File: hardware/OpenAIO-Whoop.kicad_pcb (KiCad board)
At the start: 6 copper layers, 30.3 x 30.3 mm, 250 parts, among them J1 U.FL, J10 M3, J13 M4, J2 +, J20 LED, J21 5V, J22 BZ-, J23 CAM, J24 5V, J25 GND, J26 VHD, J27 GND, J28 TX0, J29 RX0, J3 -, J31 USB, J32 CAM, J33 GND, J4 M1, J7 M2, Q26 AP1606, Q27 BC857BM, Q28 AP1606, Q29 AGM210MAP, Q30 AGM210MAP, Q31 AGM210MAP, Q32 AGM210MAP, Q33 AGM210MAP, Q34 AGM210MAP, Q35 AGM210MAP, Q36 AGM210MAP, Q37 AGM210MAP, Q38 AGM210MAP, Q39 AGM210MAP, Q40 AGM210MAP, SW1 SKUBAAE010, U1 INA186A3, U10 RP2354A, U11 BMI270, U12 TPS7A2018, U13 PY25Q128HA-DFH-IR, U14 SN74LVC1G3157, U15 TLV7031, U16 ESP32-PICO-V3, U18 SX1281, U19 RTC6705, U2 TPS61022, U20 SE5004L, U21 LP5912-3.3, U22 LP5907-2.85, U4 LP5912-3.3, U6 EFM8BB51F16I, U7 EFM8BB51F16I, U8 EFM8BB51F16I, U9 EFM8BB51F16I, X1 12MHz, X3 52MHz TCXO, X4 8MHz 10pF

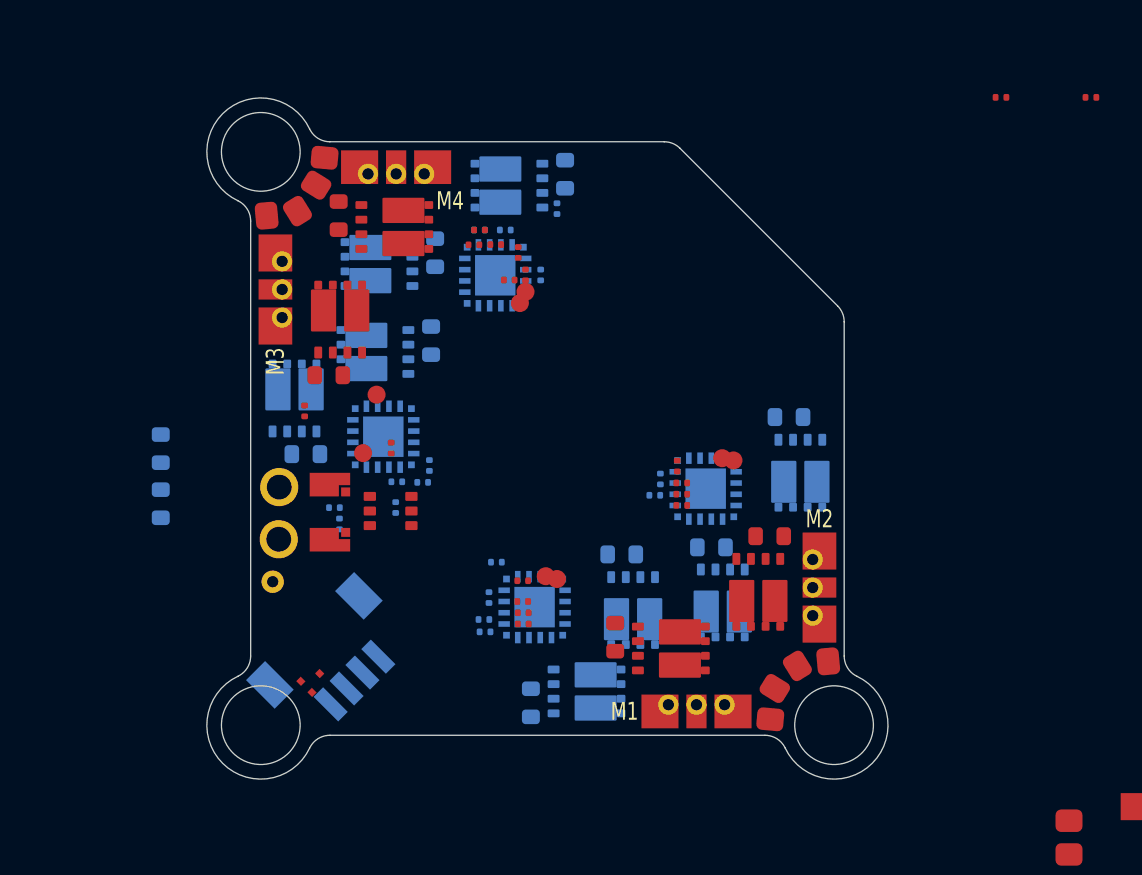
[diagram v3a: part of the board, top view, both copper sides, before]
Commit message: Owner routing checkpoint: ESC3 and ESC4 routed
Co-Authored-By: Claude Opus 5.5 <noreply@anthropic.com>
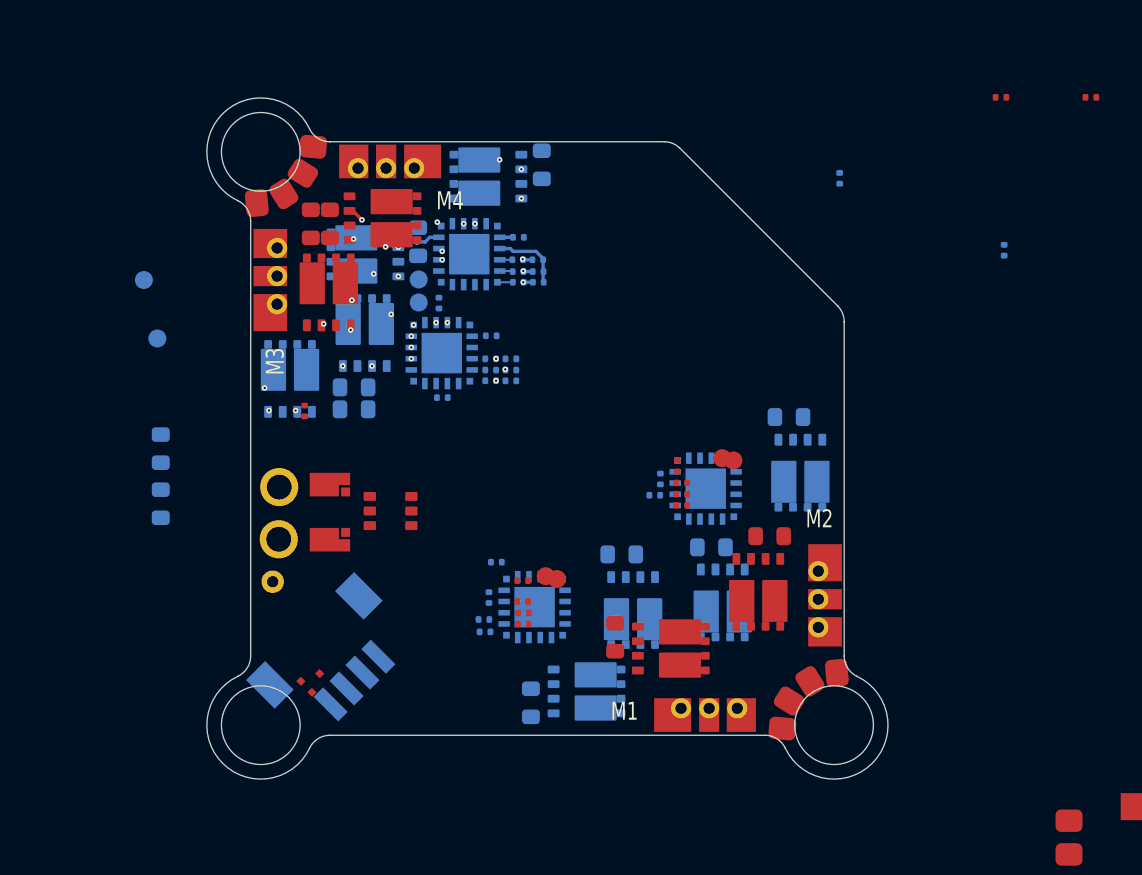
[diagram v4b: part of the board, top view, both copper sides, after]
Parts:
- C19, C31, Q37, R32, R34, R35, R38, R39, TP5, TP6, TP7, TP8: moved to B.Cu
- Q36: moved to F.Cu
- moved C25 20.6 mm to (133.5, 104.8)
- moved R33 15.0 mm to (111.9, 104.2), turned to 180 degrees
- moved C19 14.6 mm to (126.2, 101.6)
- moved TP5 11.5 mm to (95.2, 106.2), turned to 180 degrees
- moved TP6 10.5 mm to (95.8, 108.8), turned to 180 degrees
- moved R29 9.26 mm to (110.7, 110.2), turned to 180 degrees
- moved R26 8.74 mm to (110.7, 108.6), turned to 180 degrees
- moved R28 8.13 mm to (110.7, 110.6), turned to 180 degrees
- moved R27 6.88 mm to (110.7, 109.7)
- moved C33 6.78 mm to (102.7, 103.7), turned to 90 degrees
- moved R30 6.75 mm to (111.6, 109.7)
- moved C37 6.72 mm to (108.4, 107.2), turned to -90 degrees
- moved R32 6.36 mm to (111.6, 110.2), turned to 0 degrees
- moved C31 6.02 mm to (108.5, 111.4), turned to 0 degrees
- moved R31 5.23 mm to (111.6, 110.6), turned to 0 degrees
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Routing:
- net /ESC3/PHASE_A: track 0.00 -> 13.0 mm, vias 0 -> 2
- net /ESC4/PHASE_B: track 0.00 -> 10.6 mm, vias 0 -> 2
- net /ESC3/PHASE_B: track 0.00 -> 10.3 mm, vias 0 -> 2
- net /ESC3/A_COM: track 0.00 -> 9.79 mm, vias 0 -> 2
- net /ESC3/A_PWM: track 0.00 -> 9.14 mm, vias 0 -> 2
- net /ESC4/PHASE_A: track 0.00 -> 7.72 mm, vias 0 -> 2
- net /ESC4/PHASE_C: track 0.00 -> 7.27 mm, vias 0 -> 2
- net /ESC3/PHASE_C: track 0.00 -> 6.41 mm, vias 0 -> 2
- net /ESC4/C_PWM: track 0.00 -> 5.49 mm, vias 0 -> 2
- net /ESC4/C_COM: track 0.00 -> 4.65 mm, vias 0 -> 2
- net /ESC4/A_PWM: track 0.00 -> 4.37 mm, vias 0 -> 2
- net /ESC4/B_PWM: track 0.00 -> 4.34 mm, vias 0 -> 2
- net /ESC4/A_COM: track 0.00 -> 4.14 mm, vias 0 -> 2
- net /ESC3/B_PWM: track 0.00 -> 4.05 mm, vias 0 -> 2
- net /ESC4/B_COM: track 0.00 -> 3.93 mm, vias 0 -> 2
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- removed copper zone on In3.Cu, net +BATT
- removed copper zone on In1.Cu, net GND
- removed copper zone on In4.Cu, net GND

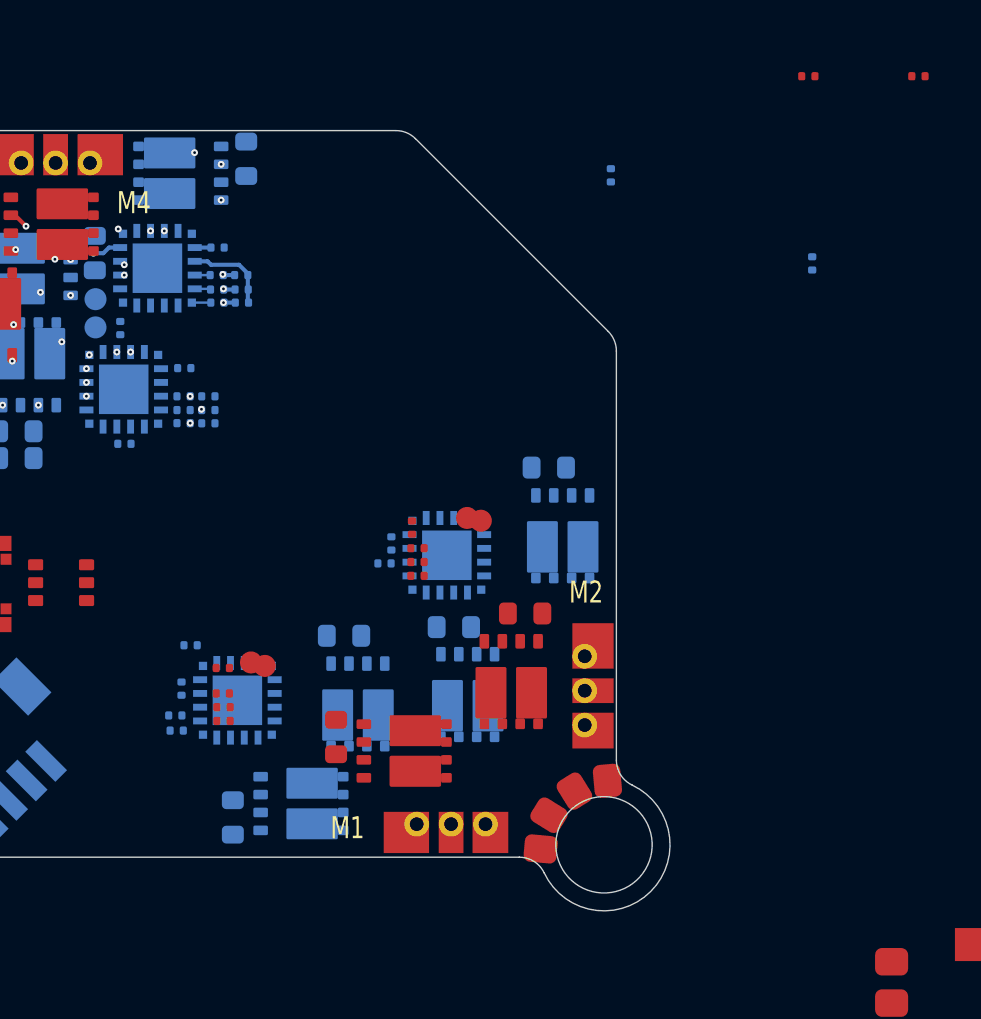
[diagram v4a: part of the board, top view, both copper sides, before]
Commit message: Copy ESC3/ESC4 placement and routing to ESC2/ESC1 (180 deg about the board centre)
The motor plugs are 180-degree symmetric about (113.211, 113.175)
(J10->J7, J13->J4, < 0.08 mm), so ESC3 -> ESC2 and ESC4 -> ESC1 by
symbol: footprints rotated 180, same side; tracks and vias duplicated
with nets renamed. Pads match their rotated source exactly; DRC per
channel pair is identical.

Co-Authored-By: Claude Opus 5.5 <noreply@anthropic.com>
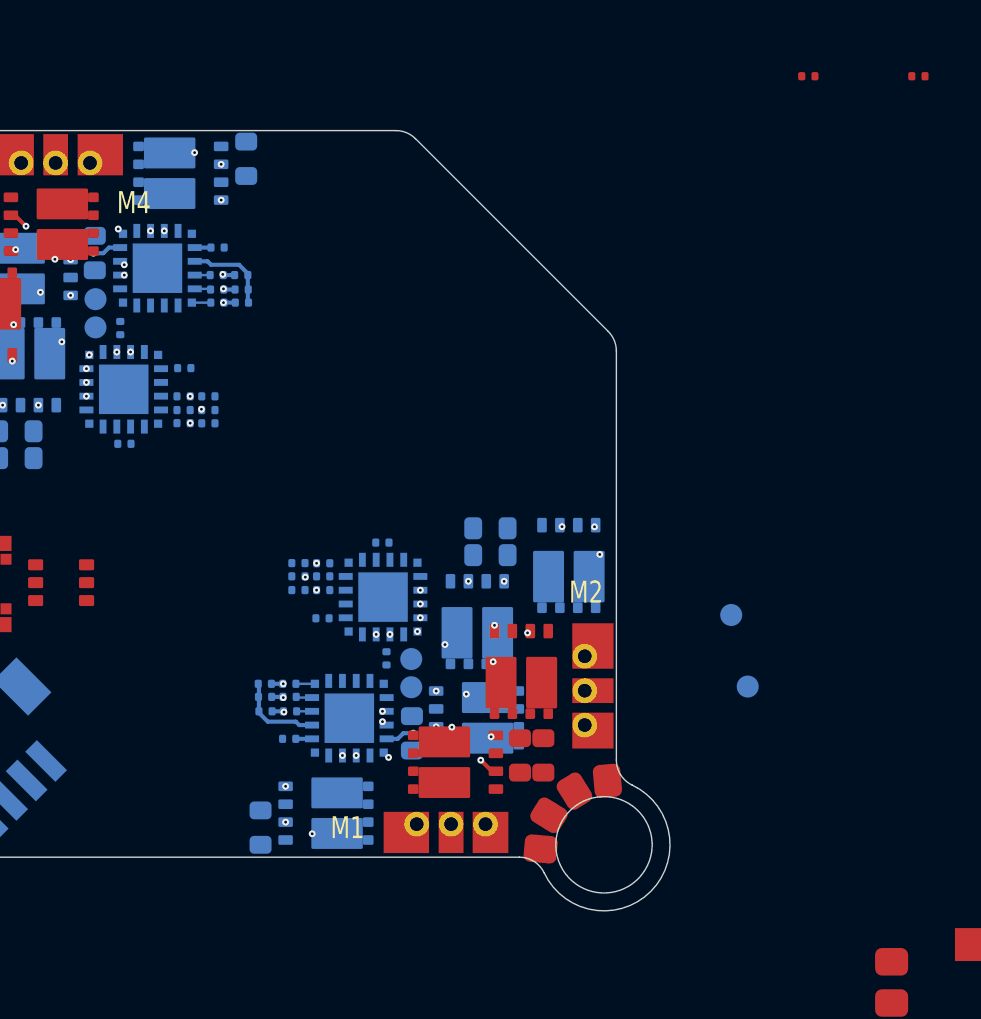
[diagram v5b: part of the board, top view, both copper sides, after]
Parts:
- C21, Q29, Q34, R13, R14, R16, R17, R20, R21, R23, R24, TP1, TP2, TP3, TP4: moved to B.Cu
- C23, Q30, Q33: moved to F.Cu
- moved C19 19.4 mm to (118.0, 119.2)
- moved C25 18.6 mm to (117.9, 115.0), turned to 180 degrees
- moved TP3 11.4 mm to (131.2, 120.2)
- moved C23 10.7 mm to (122.9, 122.7)
- moved TP4 10.2 mm to (130.6, 117.6)
- moved C20 7.60 mm to (113.5, 125.3), turned to -90 degrees
- moved TP2 5.82 mm to (118.9, 119.2), turned to -90 degrees
- moved TP1 5.38 mm to (118.9, 120.2), turned to -90 degrees
- moved C27 5.20 mm to (123.7, 122.7), turned to -90 degrees
- moved R19 4.89 mm to (115.7, 117.7), turned to 0 degrees
- moved R23 4.45 mm to (114.8, 116.7)
- moved R24 4.35 mm to (114.8, 115.7)
- moved R12 4.22 mm to (114.5, 122.1)
- moved Q30 4.13 mm to (120.6, 123.0), turned to 180 degrees
- moved U6 4.12 mm to (116.7, 121.3)
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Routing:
- net /ESC2/PHASE_A: track 0.00 -> 13.0 mm, vias 0 -> 2
- net /ESC1/PHASE_B: track 0.00 -> 10.6 mm, vias 0 -> 2
- net /ESC2/PHASE_B: track 0.00 -> 10.3 mm, vias 0 -> 2
- net /ESC2/A_COM: track 0.00 -> 9.79 mm, vias 0 -> 2
- net /ESC2/A_PWM: track 0.00 -> 9.14 mm, vias 0 -> 2
- net /ESC1/PHASE_A: track 0.00 -> 7.72 mm, vias 0 -> 2
- net /ESC1/PHASE_C: track 0.00 -> 7.27 mm, vias 0 -> 2
- net /ESC2/PHASE_C: track 0.00 -> 6.41 mm, vias 0 -> 2
- net /ESC1/C_PWM: track 0.00 -> 5.49 mm, vias 0 -> 2
- net /ESC1/C_COM: track 0.00 -> 4.65 mm, vias 0 -> 2
- net /ESC1/A_PWM: track 0.00 -> 4.37 mm, vias 0 -> 2
- net /ESC1/B_PWM: track 0.00 -> 4.34 mm, vias 0 -> 2
- net /ESC1/A_COM: track 0.00 -> 4.14 mm, vias 0 -> 2
- net /ESC2/B_PWM: track 0.00 -> 4.05 mm, vias 0 -> 2
- net /ESC1/B_COM: track 0.00 -> 3.93 mm, vias 0 -> 2
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
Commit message: Owner routing checkpoint before the In4 -> In2 conversion
Co-Authored-By: Claude Opus 5.5 <noreply@anthropic.com>
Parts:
- moved Q36 0.28 mm to (103.8, 106.7)
- moved Q33 0.19 mm to (122.8, 119.7)
- moved C23 0.10 mm to (122.9, 122.6)
- moved C27 0.10 mm to (123.7, 122.6)
- moved C33 0.07 mm to (102.7, 103.7)
- moved C41 0.07 mm to (103.5, 103.7)
- turned J22 to -174.8 degrees

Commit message: ESC3/ESC4 inner routing moved In4 -> In2 and recopied to ESC2/ESC1
In4 (L5) is the GND plane: 76 tracks moved to In2; 8 blind F-In4 vias
became F-In1 microvias; 35 buried In1-In4 vias added 0.25 mm from their
microvia, track ends moved onto them. ESC2/ESC1 recopied (180 deg).
Remaining per channel: clearance and hole spacing at some new buried
vias, one ESC3/ESC2 through via (manual).

Co-Authored-By: Claude Opus 5.5 <noreply@anthropic.com>
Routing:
- net /ESC4/C_PWM: track 5.49 -> 4.99 mm, vias 2 -> 4
- net /ESC4/A_COM: track 4.14 -> 3.64 mm, vias 2 -> 4
- net /ESC3/PHASE_C: track 6.41 -> 5.91 mm, vias 2 -> 4
- net /ESC2/PHASE_C: track 6.41 -> 5.91 mm, vias 2 -> 4
- net /ESC1/C_PWM: track 5.49 -> 4.99 mm, vias 2 -> 4
- net /ESC1/A_COM: track 4.14 -> 3.64 mm, vias 2 -> 4
- net /ESC1/C_COM: track 4.65 -> 4.15 mm, vias 2 -> 4
- net /ESC4/C_COM: track 4.65 -> 4.15 mm, vias 2 -> 4
- net /ESC4/PHASE_B: track 10.6 -> 10.1 mm, vias 2 -> 4
- net /ESC1/PHASE_B: track 10.6 -> 10.1 mm, vias 2 -> 4
- net /ESC2/C_PWM: track 2.09 -> 1.59 mm, vias 2 -> 4
- net /ESC3/C_PWM: track 2.09 -> 1.59 mm, vias 2 -> 4
- net /ESC3/PHASE_A: track 13.0 -> 12.5 mm, vias 2 -> 4
- net /ESC2/PHASE_A: track 13.0 -> 12.5 mm, vias 2 -> 4
- net /ESC3/PHASE_B: track 10.3 -> 9.82 mm, vias 2 -> 4
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
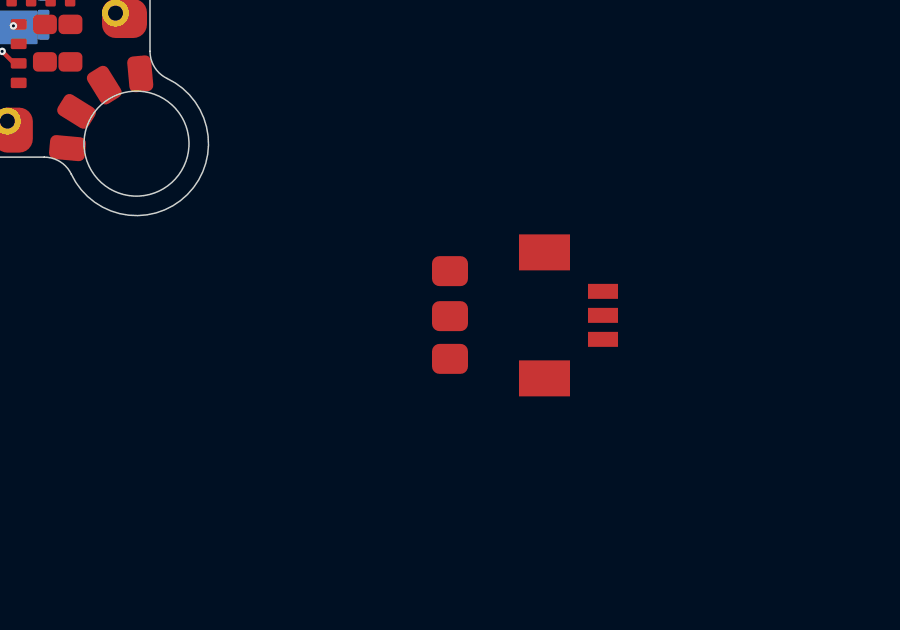
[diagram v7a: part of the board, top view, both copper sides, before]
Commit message: Planes and rule areas restored and refilled, owner pad edits, stackup note on the board
L2_GND / L4_BATT / L5_GND planes and the 24 rule areas copied back (the
saved board had none) and refilled. Owner footprint edits kept: motor
solder lands narrowed and rounded, SolderPad_1.0x1.2mm lands 0.8 x 1.2;
land specs follow them (PASS); the 15 placed copies refreshed in place.
setup_board run: stackup / routing note on User.Comments. KiCad's
cosmetic schematic re-save discarded (netlist and values equal to HEAD).

setup_board --check up to date; board_spec 31/31; sync dry run 0;
ERC 0 errors; check_netlist 7 ok.

Co-Authored-By: Claude Opus 5.5 <noreply@anthropic.com>
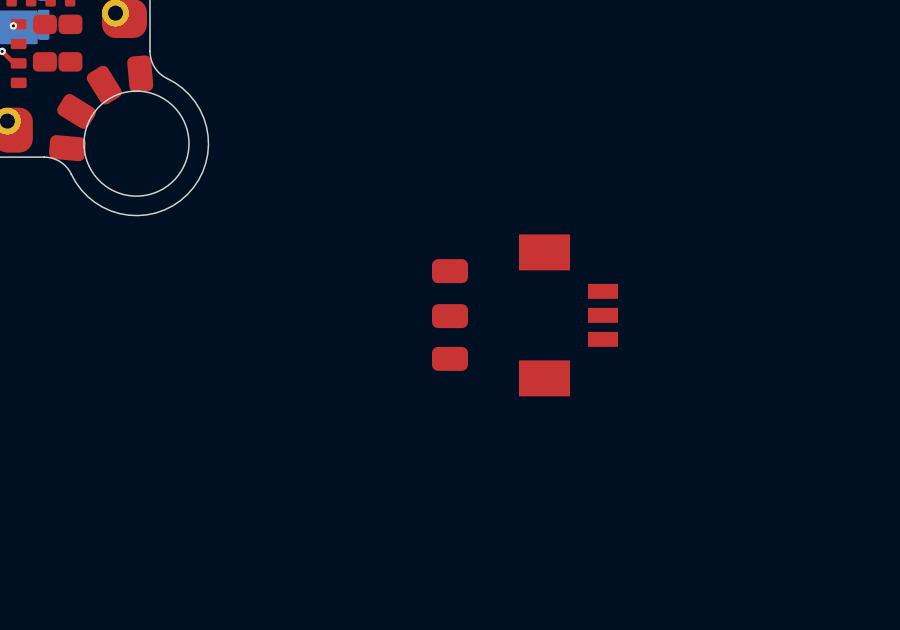
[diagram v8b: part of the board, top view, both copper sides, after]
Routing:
- added copper zone on In3.Cu, net +BATT
- added copper zone on In1.Cu, net GND
- added copper zone on In4.Cu, net GND
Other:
- board text added: "STACKUP NextPCB 06101103-1080, 6L HDI 1+4+1, 1.0 mm, FR-4 Dk 4.2 L1 F.Cu 1 oz parts, RF 50R CPWG 0.105/0.15, hot loops, fan-out 1080 0.077 laser microvia L1-L2 0.10/0.25, in pad L2 In1 1 oz* solid GND plane, no tracks 1080 0.077 (* plated foil) L3 In2 1 oz signal layer, refs L2; no Analog / RF core 0.536 buried via L2-L5 0.15/0.35 (power 0.20/0.40) L4 In3 1 oz +BATT plane, refs L5; no Analog / RF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"
- board text removed: "F.Cu sig | In1 GND | In2 sig | In3 +BATT/PWR | In4 GND | B.Cu sig"
